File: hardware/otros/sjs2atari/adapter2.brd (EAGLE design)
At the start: 12.8 x 9.6 mm, 2 parts

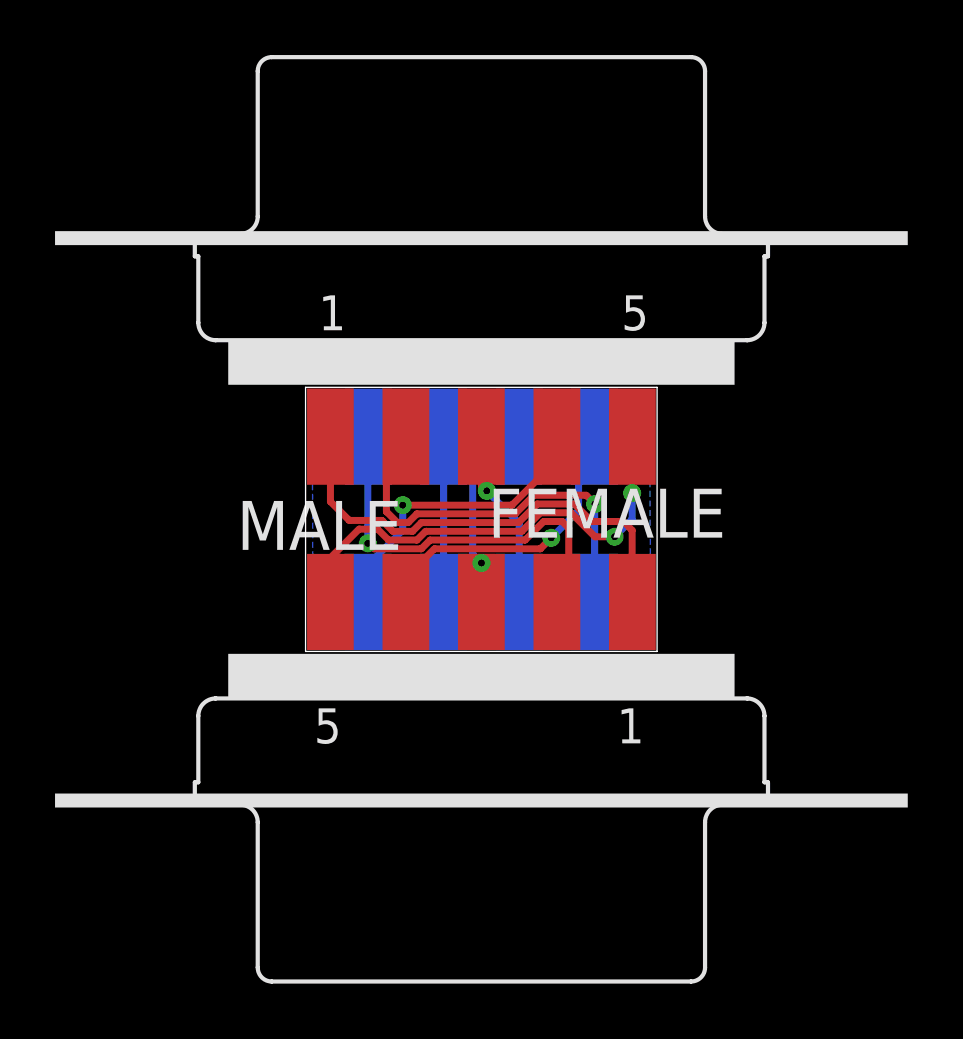
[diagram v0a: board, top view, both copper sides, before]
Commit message: 
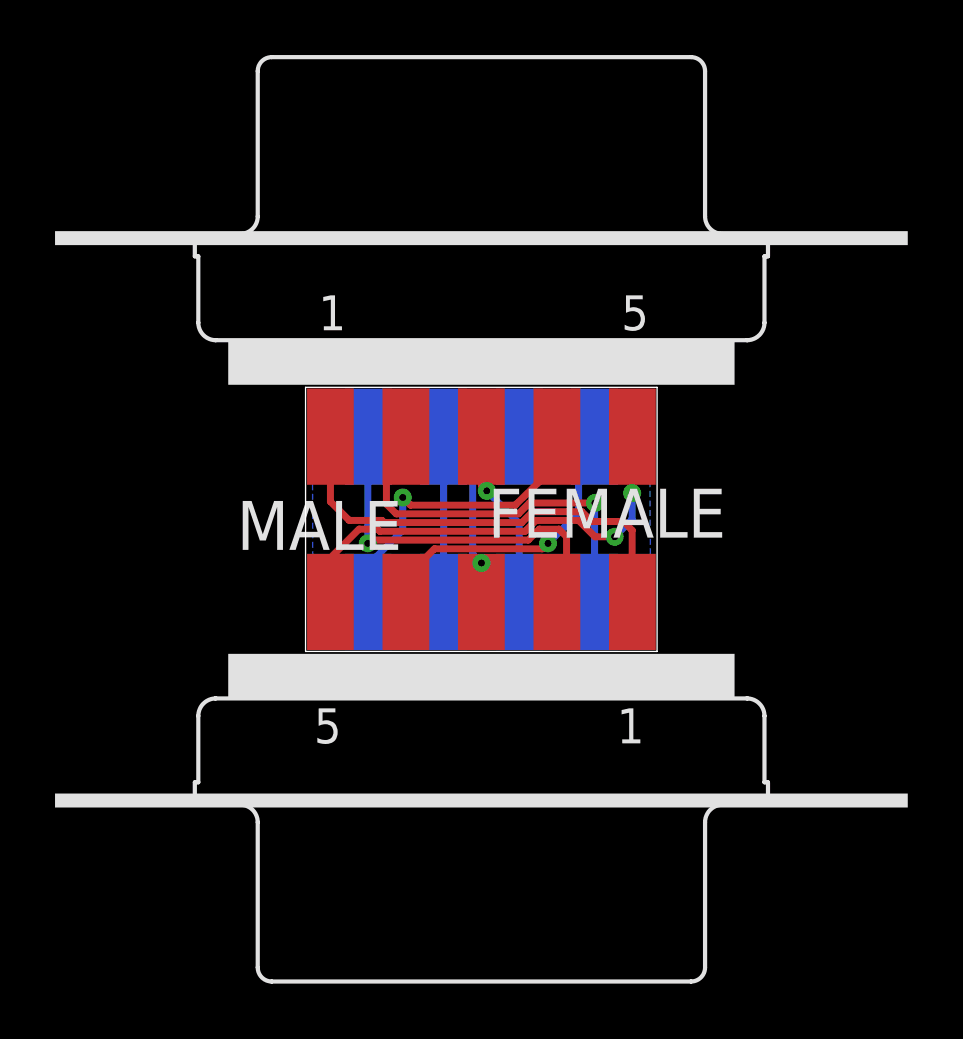
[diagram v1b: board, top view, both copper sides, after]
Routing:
- net P4_6: track 14.9 -> 14.2 mm
- net P9_2: track 15.8 -> 15.2 mm
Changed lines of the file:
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@@
 <wire x1="6.4641" y1="2.790425" x2="6.4641" y2="3.685975" width="0.254" layer="1"/>
 <wire x1="6.4641" y1="3.685975" x2="7.5009375" y2="4.7228125" width="0.254" layer="1"/>
-<wire x1="7.5009375" y1="4.7228125" x2="11.350625" y2="4.7228125" width="0.254" layer="1"/>
-<wire x1="11.350625" y1="4.7228125" x2="11.7475" y2="5.1196875" width="0.254" layer="1"/>
-<via x="11.7475" y="5.1196875" extent="1-16" drill="0.25"/>
-<wire x1="11.7475" y1="5.1196875" x2="12.7396875" y2="6.111875" width="0.254" layer="16"/>
-<wire x1="12.7396875" y1="6.111875" x2="12.7396875" y2="8.2153125" width="0.254" layer="16"/>
+<wire x1="7.5009375" y1="4.7228125" x2="11.43" y2="4.7228125" width="0.254" layer="1"/>
+<via x="11.6284375" y="4.92125" extent="1-16" drill="0.25"/>
+<wire x1="12.7396875" y1="6.0325" x2="12.7396875" y2="8.2153125" width="0.254" layer="16"/>
 <wire x1="12.7396875" y1="8.2153125" x2="13.3223" y2="8.797925" width="0.254" layer="16"/>
+<wire x1="11.43" y1="4.7228125" x2="11.6284375" y2="4.92125" width="0.254" layer="1"/>
+<wire x1="12.7396875" y1="6.0325" x2="11.6284375" y2="4.92125" width="0.254" layer="16"/>
 </signal>
 <signal name="P4_6">
@@
 <wire x1="6.4690625" y1="8.7933625" x2="6.4641" y2="8.798325" width="0.254" layer="1"/>
 <wire x1="13.3223" y1="2.790825" x2="13.3223" y2="6.3373" width="0.254" layer="16"/>
-<wire x1="13.3223" y1="6.3373" x2="13.335" y2="6.35" width="0.254" layer="16"/>
-<via x="13.335" y="6.35" extent="1-16" drill="0.25"/>
-<wire x1="6.1515625" y1="5.6753125" x2="5.7546875" y2="6.0721875" width="0.254" layer="1"/>
-<wire x1="5.7546875" y1="6.0721875" x2="5.7546875" y2="8.0889125" width="0.254" layer="1"/>
+<wire x1="13.3223" y1="6.3373" x2="13.335" y2="6.3896875" width="0.254" layer="16"/>
+<via x="13.335" y="6.3896875" extent="1-16" drill="0.25"/>
 <wire x1="5.7546875" y1="8.0889125" x2="6.4641" y2="8.798325" width="0.254" layer="1"/>
-<wire x1="6.1515625" y1="5.6753125" x2="6.5484375" y2="5.6753125" width="0.254" layer="1"/>
-<wire x1="6.5484375" y1="5.6753125" x2="6.8659375" y2="5.9928125" width="0.254" layer="1"/>
-<wire x1="6.8659375" y1="5.9928125" x2="10.4378125" y2="5.9928125" width="0.254" layer="1"/>
-<wire x1="10.4378125" y1="5.9928125" x2="11.1125" y2="6.6675" width="0.254" layer="1"/>
-<wire x1="11.1125" y1="6.6675" x2="13.0175" y2="6.6675" width="0.254" layer="1"/>
-<wire x1="13.0175" y1="6.6675" x2="13.335" y2="6.35" width="0.254" layer="1"/>
+<wire x1="6.111875" y1="5.9928125" x2="10.556875" y2="5.9928125" width="0.254" layer="1"/>
+<wire x1="6.111875" y1="5.9928125" x2="5.7546875" y2="6.35" width="0.254" layer="1"/>
+<wire x1="5.7546875" y1="6.35" x2="5.7546875" y2="8.0889125" width="0.254" layer="1"/>
+<wire x1="10.556875" y1="5.9928125" x2="10.95375" y2="6.3896875" width="0.254" layer="1"/>
+<wire x1="13.335" y1="6.3896875" x2="10.95375" y2="6.3896875" width="0.254" layer="1"/>
 </signal>
 <signal name="P5_1">
@@
 <wire x1="3.7213" y1="6.4387" x2="4.4053125" y2="5.7546875" width="0.254" layer="1"/>
 <wire x1="4.4053125" y1="5.7546875" x2="5.5959375" y2="5.7546875" width="0.254" layer="1"/>
-<wire x1="5.5959375" y1="5.7546875" x2="5.9928125" y2="5.3578125" width="0.254" layer="1"/>
-<wire x1="5.9928125" y1="5.3578125" x2="6.7071875" y2="5.3578125" width="0.254" layer="1"/>
-<wire x1="6.7071875" y1="5.3578125" x2="7.0246875" y2="5.6753125" width="0.254" layer="1"/>
 <wire x1="14.366875" y1="5.715" x2="14.684375" y2="5.3975" width="0.254" layer="1"/>
 <wire x1="14.684375" y1="5.3975" x2="14.684375" y2="2.79975" width="0.254" layer="1"/>
 <wire x1="14.684375" y1="2.79975" x2="14.6937" y2="2.790425" width="0.254" layer="1"/>
-<wire x1="7.0246875" y1="5.6753125" x2="10.556875" y2="5.6753125" width="0.254" layer="1"/>
-<wire x1="10.556875" y1="5.6753125" x2="11.2315625" y2="6.35" width="0.254" layer="1"/>
-<wire x1="11.2315625" y1="6.35" x2="12.5809375" y2="6.35" width="0.254" layer="1"/>
-<wire x1="12.5809375" y1="6.35" x2="13.2159375" y2="5.715" width="0.254" layer="1"/>
+<wire x1="5.6753125" y1="5.6753125" x2="10.6759375" y2="5.6753125" width="0.254" layer="1"/>
 <wire x1="13.2159375" y1="5.715" x2="14.366875" y2="5.715" width="0.254" layer="1"/>
+<wire x1="5.6753125" y1="5.6753125" x2="5.5959375" y2="5.7546875" width="0.254" layer="1"/>
+<wire x1="10.6759375" y1="5.6753125" x2="11.0728125" y2="6.0721875" width="0.254" layer="1"/>
+<wire x1="11.0728125" y1="6.0721875" x2="12.85875" y2="6.0721875" width="0.254" layer="1"/>
+<wire x1="12.85875" y1="6.0721875" x2="13.2159375" y2="5.715" width="0.254" layer="1"/>
 </signal>
 <signal name="P9_2">
 <contactref element="FEMALE" pad="2"/>
 <contactref element="MALE" pad="6"/>
-<wire x1="5.318125" y1="4.7228125" x2="5.08" y2="4.92125" width="0.254" layer="1"/>
 <via x="5.08" y="4.92125" extent="1-16" drill="0.25"/>
 <wire x1="5.08" y1="4.92125" x2="5.08" y2="8.785225" width="0.254" layer="16"/>
 <wire x1="5.08" y1="8.785225" x2="5.0927" y2="8.797925" width="0.254" layer="16"/>
-<wire x1="5.318125" y1="4.7228125" x2="7.0246875" y2="4.7228125" width="0.254" layer="1"/>
-<wire x1="7.0246875" y1="4.7228125" x2="7.3421875" y2="5.0403125" width="0.254" layer="1"/>
-<wire x1="7.3421875" y1="5.0403125" x2="10.795" y2="5.0403125" width="0.254" layer="1"/>
-<wire x1="10.795" y1="5.0403125" x2="11.4696875" y2="5.715" width="0.254" layer="1"/>
+<wire x1="5.1990625" y1="5.0403125" x2="10.9140625" y2="5.0403125" width="0.254" layer="1"/>
 <wire x1="11.9509" y1="2.790425" x2="11.9509" y2="3.0609" width="0.254" layer="1"/>
 <wire x1="11.9509" y1="3.0609" x2="12.5809375" y2="3.6909375" width="0.254" layer="1"/>
-<wire x1="11.4696875" y1="5.715" x2="12.144375" y2="5.715" width="0.254" layer="1"/>
-<wire x1="12.144375" y1="5.715" x2="12.3825" y2="5.476875" width="0.254" layer="1"/>
-<wire x1="12.3825" y1="5.476875" x2="12.3825" y2="3.222025" width="0.254" layer="1"/>
 <wire x1="12.3825" y1="3.222025" x2="11.9509" y2="2.790425" width="0.254" layer="1"/>
+<wire x1="5.1990625" y1="5.0403125" x2="5.08" y2="4.92125" width="0.254" layer="1"/>
+<wire x1="10.9140625" y1="5.0403125" x2="11.3109375" y2="5.4371875" width="0.254" layer="1"/>
+<wire x1="11.3109375" y1="5.4371875" x2="12.0253125" y2="5.4371875" width="0.254" layer="1"/>
+<wire x1="12.0253125" y1="5.4371875" x2="12.303125" y2="5.159375" width="0.254" layer="1"/>
+<wire x1="12.303125" y1="5.159375" x2="12.303125" y2="3.3014" width="0.254" layer="1"/>
+<wire x1="12.303125" y1="3.3014" x2="12.3825" y2="3.222025" width="0.254" layer="1"/>
 </signal>
 <signal name="P3_7">
@@
 <contactref element="FEMALE" pad="9"/>
 <contactref element="MALE" pad="4"/>
-<wire x1="11.9509" y1="8.798325" x2="11.9509" y2="7.9424625" width="0.254" layer="1"/>
-<via x="6.35" y="6.3103125" extent="1-16" drill="0.25"/>
+<wire x1="11.9509" y1="8.798325" x2="11.9509" y2="7.7837125" width="0.254" layer="1"/>
+<via x="6.35" y="6.588125" extent="1-16" drill="0.25"/>
 <wire x1="5.0927" y1="2.790825" x2="5.0927" y2="4.1402" width="0.254" layer="16"/>
-<wire x1="6.35" y1="6.3103125" x2="10.31875" y2="6.3103125" width="0.254" layer="1"/>
-<wire x1="10.31875" y1="6.3103125" x2="11.9509" y2="7.9424625" width="0.254" layer="1"/>
+<wire x1="10.4378125" y1="6.3103125" x2="11.9509" y2="7.7837125" width="0.254" layer="1"/>
 <wire x1="5.0927" y1="4.1402" x2="6.35" y2="5.3975" width="0.254" layer="16"/>
-<wire x1="6.35" y1="5.3975" x2="6.35" y2="6.3103125" width="0.254" layer="16"/>
+<wire x1="6.35" y1="5.3975" x2="6.35" y2="6.588125" width="0.254" layer="16"/>
+<wire x1="10.4378125" y1="6.3103125" x2="6.6278125" y2="6.3103125" width="0.254" layer="1"/>
+<wire x1="6.6278125" y1="6.3103125" x2="6.35" y2="6.588125" width="0.254" layer="1"/>
 </signal>
 <signal name="P1_5">
@@
 <wire x1="14.684375" y1="5.794375" x2="14.049375" y2="5.159375" width="0.254" layer="16"/>
 <wire x1="4.7625" y1="5.4371875" x2="5.4371875" y2="5.4371875" width="0.254" layer="1"/>
-<wire x1="5.4371875" y1="5.4371875" x2="5.8340625" y2="5.0403125" width="0.254" layer="1"/>
-<wire x1="5.8340625" y1="5.0403125" x2="6.8659375" y2="5.0403125" width="0.254" layer="1"/>
-<wire x1="6.8659375" y1="5.0403125" x2="7.1834375" y2="5.3578125" width="0.254" layer="1"/>
-<wire x1="7.1834375" y1="5.3578125" x2="10.6759375" y2="5.3578125" width="0.254" layer="1"/>
-<wire x1="10.6759375" y1="5.3578125" x2="11.350625" y2="6.0325" width="0.254" layer="1"/>
-<wire x1="11.350625" y1="6.0325" x2="12.461875" y2="6.0325" width="0.254" layer="1"/>
-<wire x1="12.461875" y1="6.0325" x2="13.335" y2="5.159375" width="0.254" layer="1"/>
+<wire x1="5.5165625" y1="5.3578125" x2="10.795" y2="5.3578125" width="0.254" layer="1"/>
 <wire x1="14.049375" y1="5.159375" x2="13.335" y2="5.159375" width="0.254" layer="1"/>
+<wire x1="5.5165625" y1="5.3578125" x2="5.4371875" y2="5.4371875" width="0.254" layer="1"/>
+<wire x1="10.795" y1="5.3578125" x2="11.191875" y2="5.7546875" width="0.254" layer="1"/>
+<wire x1="11.191875" y1="5.7546875" x2="12.7396875" y2="5.7546875" width="0.254" layer="1"/>
+<wire x1="12.7396875" y1="5.7546875" x2="13.335" y2="5.159375" width="0.254" layer="1"/>
 </signal>
 <signal name="N$1">
